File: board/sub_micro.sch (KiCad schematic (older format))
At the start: 0 parts

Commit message: More progress on the schematic. 6502 Done.
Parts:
- added J401: USB_B, symbol Connector_Specialized:USB_B
- added U401: STM32F072CBTx, Package_QFP:LQFP-48_7x7mm_P0.5mm, symbol MCU_ST_STM32:STM32F072CBTx
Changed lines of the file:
@@
 $Descr A4 11693 8268
 encoding utf-8
-Sheet 1 8
+Sheet 3 10
 Title ""
 Date ""
@@
 Comment4 ""
 $EndDescr
+$Comp
+L MCU_ST_STM32:STM32F072CBTx U401
+U 1 1 5AA35B88
+P 5400 3150
+F 0 "U401" H 5400 5228 50  0000 C CNN
+F 1 "STM32F072CBTx" H 5400 5137 50  0000 C CNN
+F 2 "Package_QFP:LQFP-48_7x7mm_P0.5mm" H 9100 4925 50  0001 R TNN
+F 3 "http://www.st.com/st-web-ui/static/active/en/resource/technical/document/datasheet/DM00090510.pdf" H 5400 3150 50  0001 C CNN
+	1    5400 3150
+	1    0    0    -1
+$EndComp
+$Comp
+L Connector_Specialized:USB_B J401
+U 1 1 5AA35CDE
+P 10500 4100
+F 0 "J401" H 10271 4091 50  0000 R CNN
+F 1 "USB_B" H 10271 4000 50  0000 R CNN
+F 2 "" H 10650 4050 50  0001 C CNN
+F 3 "" H 10650 4050 50  0001 C CNN
+	1    10500 4100
+	-1   0    0    -1
+$EndComp
 $EndSCHEMATC

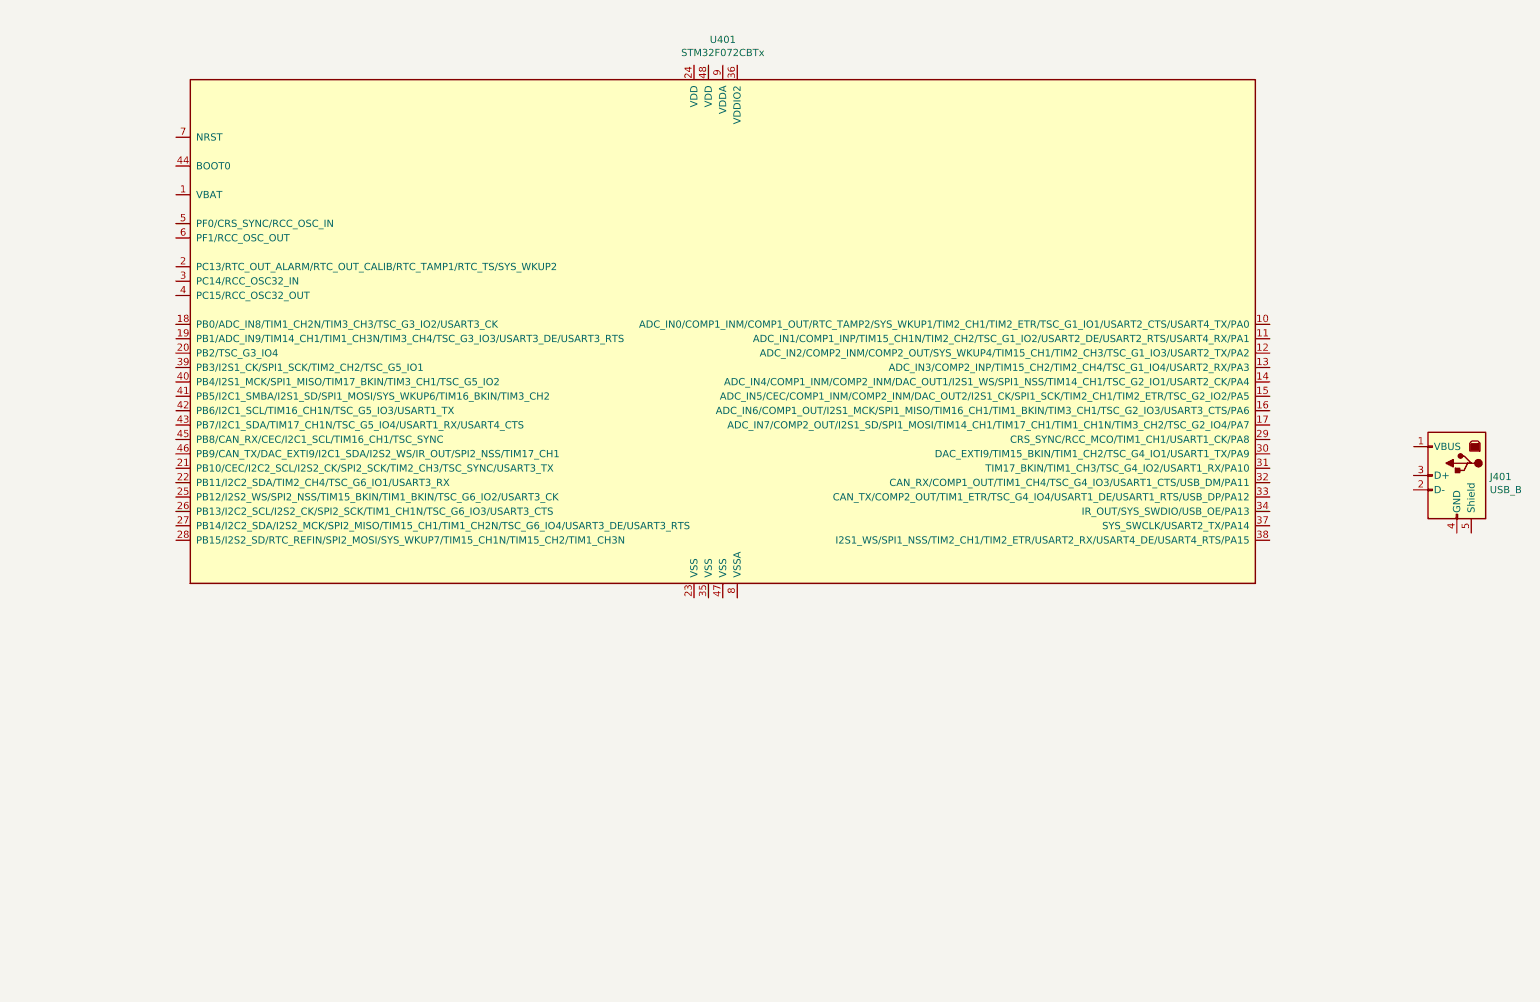
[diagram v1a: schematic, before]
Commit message: Level converters complete, display almost done
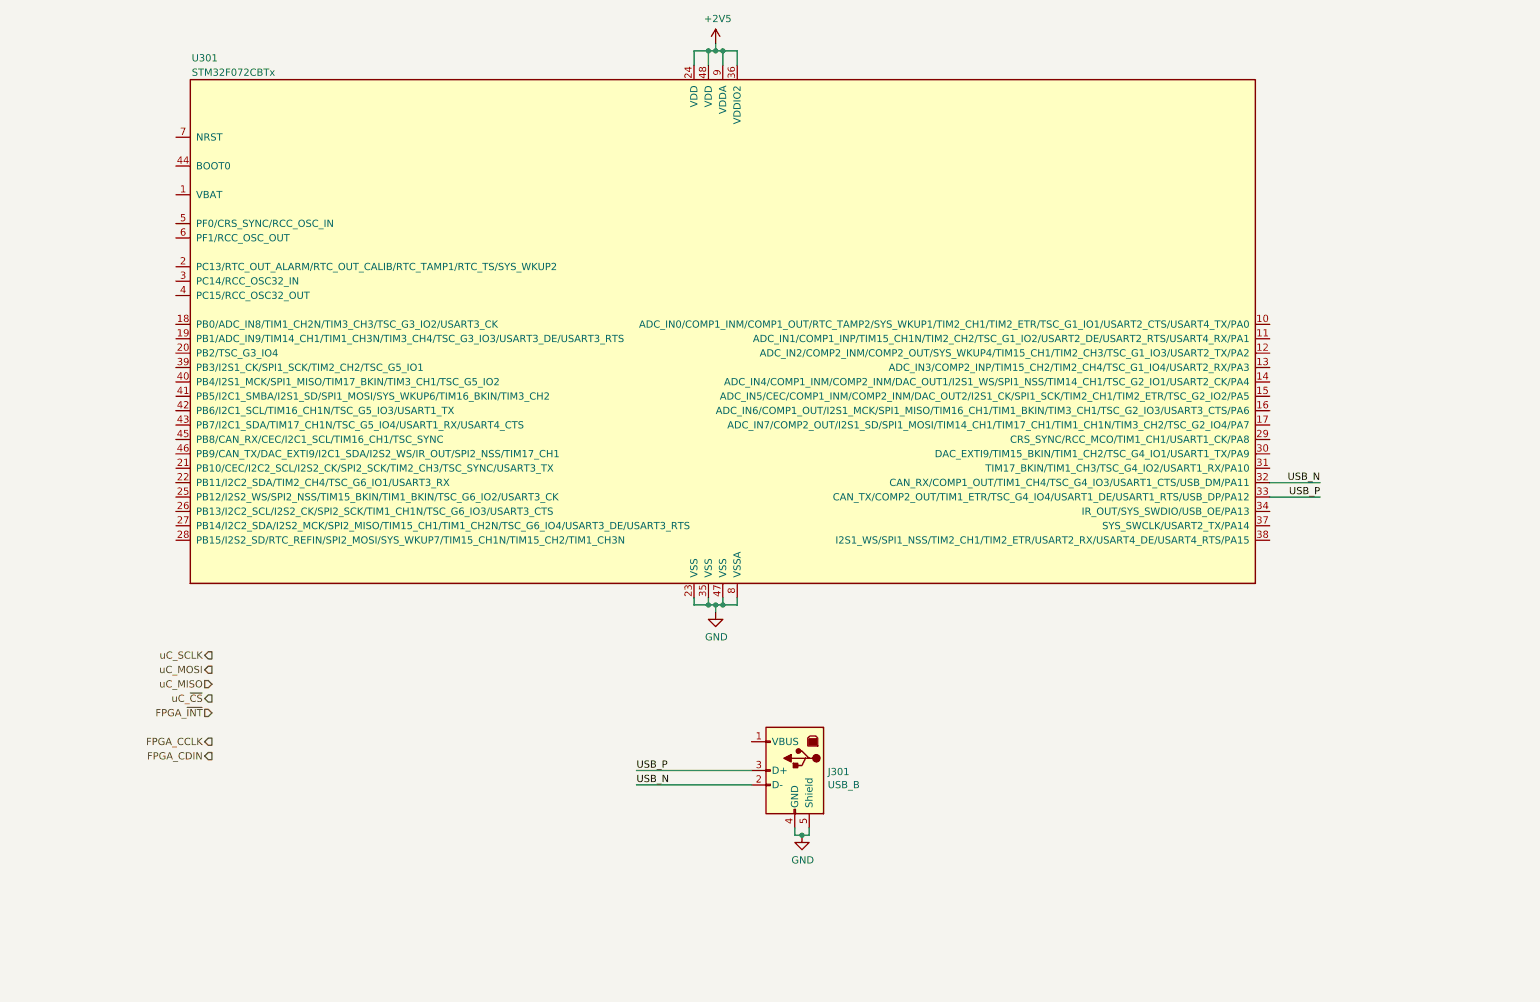
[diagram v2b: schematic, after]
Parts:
- renumbered J401 to J301, U401 to U301
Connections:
- net GND: now reaches U301.23 (VSS)
- net GND: now also J301.4 (GND), J301.5 (Shield), U301.35 (VSS), U301.47 (VSS), U301.8 (VSSA)
- net +2V5: now reaches U301.24 (VDD)
- net +2V5: now also U301.36 (VDDIO2), U301.48 (VDD), U301.9 (VDDA)
- net USB_N: now reaches U301.32 (CAN_RX/COMP1_OUT/TIM1_CH4/TSC_G4_IO3/USART1_CTS/USB_DM/PA11)
- net USB_N: now also J301.2 (D-)
- net USB_P: now reaches U301.33 (CAN_TX/COMP2_OUT/TIM1_ETR/TSC_G4_IO4/USART1_DE/USART1_RTS/USB_DP/PA12)
- net USB_P: now also J301.3 (D+)
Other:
- moved on the sheet: J301
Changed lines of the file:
@@
 $Descr A4 11693 8268
 encoding utf-8
-Sheet 3 10
+Sheet 3 15
 Title ""
 Date ""
@@
 Comment2 ""
 Comment3 ""
-Comment4 ""
+Comment4 "Quokka 6502 Microprocessor Trainer"
 $EndDescr
 $Comp
-L MCU_ST_STM32:STM32F072CBTx U401
+L MCU_ST_STM32:STM32F072CBTx U301
 U 1 1 5AA35B88
 P 5400 3150
-F 0 "U401" H 5400 5228 50  0000 C CNN
-F 1 "STM32F072CBTx" H 5400 5137 50  0000 C CNN
+F 0 "U301" H 1800 5100 50  0000 C CNN
+F 1 "STM32F072CBTx" H 2000 5000 50  0000 C CNN
 F 2 "Package_QFP:LQFP-48_7x7mm_P0.5mm" H 9100 4925 50  0001 R TNN
 F 3 "http://www.st.com/st-web-ui/static/active/en/resource/technical/document/datasheet/DM00090510.pdf" H 5400 3150 50  0001 C CNN
@@
 $EndComp
 $Comp
-L Connector_Specialized:USB_B J401
+L Connector_Specialized:USB_B J301
 U 1 1 5AA35CDE
-P 10500 4100
-F 0 "J401" H 10271 4091 50  0000 R CNN
-F 1 "USB_B" H 10271 4000 50  0000 R CNN
-F 2 "" H 10650 4050 50  0001 C CNN
-F 3 "" H 10650 4050 50  0001 C CNN
-	1    10500 4100
+P 5900 6150
+F 0 "J301" H 5671 6141 50  0000 R CNN
+F 1 "USB_B" H 5671 6050 50  0000 R CNN
+F 2 "" H 6050 6100 50  0001 C CNN
+F 3 "" H 6050 6100 50  0001 C CNN
+	1    5900 6150
 	-1   0    0    -1
 $EndComp
+Text HLabel 1850 5350 0    50   Output ~ 0
+uC_SCLK
+Text HLabel 1850 5450 0    50   Output ~ 0
+uC_MOSI
+Text HLabel 1850 5550 0    50   Input ~ 0
+uC_MISO
+Text HLabel 1850 5650 0    50   Output ~ 0
+uC_~CS
+Text HLabel 1850 5750 0    50   Input ~ 0
+FPGA_~INT
+Text Label 9550 4150 2    50   ~ 0
+USB_N
+Wire Wire Line
+	9200 4150 9550 4150
+Wire Wire Line
+	9200 4250 9550 4250
+Text Label 9550 4250 2    50   ~ 0
+USB_P
+Wire Wire Line
+	5600 6150 4800 6150
+Wire Wire Line
+	5600 6250 4800 6250
+Text Label 4800 6250 0    50   ~ 0
+USB_N
+Text Label 4800 6150 0    50   ~ 0
+USB_P
+$Comp
+L power:GND #PWR0303
+U 1 1 5AA58CA8
+P 5950 6600
+F 0 "#PWR0303" H 5950 6350 50  0001 C CNN
+F 1 "GND" H 5955 6427 50  0000 C CNN
+F 2 "" H 5950 6600 50  0001 C CNN
+F 3 "" H 5950 6600 50  0001 C CNN
+	1    5950 6600
+	1    0    0    -1
+$EndComp
+Wire Wire Line
+	5900 6550 5900 6600
+Wire Wire Line
+	5900 6600 5950 6600
+Wire Wire Line
+	5950 6600 6000 6600
+Wire Wire Line
+	6000 6600 6000 6550
+Connection ~ 5950 6600
+$Comp
+L power:+2V5 #PWR0301
+U 1 1 5AA5F4DD
+P 5350 1100
+F 0 "#PWR0301" H 5350 950 50  0001 C CNN
+F 1 "+2V5" H 5365 1273 50  0000 C CNN
+F 2 "" H 5350 1100 50  0001 C CNN
+F 3 "" H 5350 1100 50  0001 C CNN
+	1    5350 1100
+	1    0    0    -1
+$EndComp
+Wire Wire Line
+	5350 1100 5350 1150
+Wire Wire Line
+	5200 1150 5200 1250
+Wire Wire Line
+	5300 1250 5300 1150
+Wire Wire Line
+	5200 1150 5300 1150
+Connection ~ 5300 1150
+Wire Wire Line
+	5300 1150 5350 1150
+Wire Wire Line
+	5350 1150 5400 1150
+Wire Wire Line
+	5400 1150 5400 1250
+Connection ~ 5350 1150
+Wire Wire Line
+	5400 1150 5500 1150
+Wire Wire Line
+	5500 1150 5500 1250
+Connection ~ 5400 1150
+$Comp
+L power:GND #PWR0302
+U 1 1 5AA5F8A6
+P 5350 5050
+F 0 "#PWR0302" H 5350 4800 50  0001 C CNN
+F 1 "GND" H 5355 4877 50  0000 C CNN
+F 2 "" H 5350 5050 50  0001 C CNN
+F 3 "" H 5350 5050 50  0001 C CNN
+	1    5350 5050
+	1    0    0    -1
+$EndComp
+Wire Wire Line
+	5350 5050 5350 5000
+Wire Wire Line
+	5350 5000 5300 5000
+Wire Wire Line
+	5200 5000 5200 4950
+Wire Wire Line
+	5300 4950 5300 5000
+Connection ~ 5300 5000
+Wire Wire Line
+	5300 5000 5200 5000
+Wire Wire Line
+	5400 4950 5400 5000
+Wire Wire Line
+	5400 5000 5350 5000
+Connection ~ 5350 5000
+Wire Wire Line
+	5500 4950 5500 5000
+Wire Wire Line
+	5500 5000 5400 5000
+Connection ~ 5400 5000
+Text HLabel 1850 5950 0    50   Output ~ 0
+FPGA_CCLK
+Text HLabel 1850 6050 0    50   Output ~ 0
+FPGA_CDIN
 $EndSCHEMATC

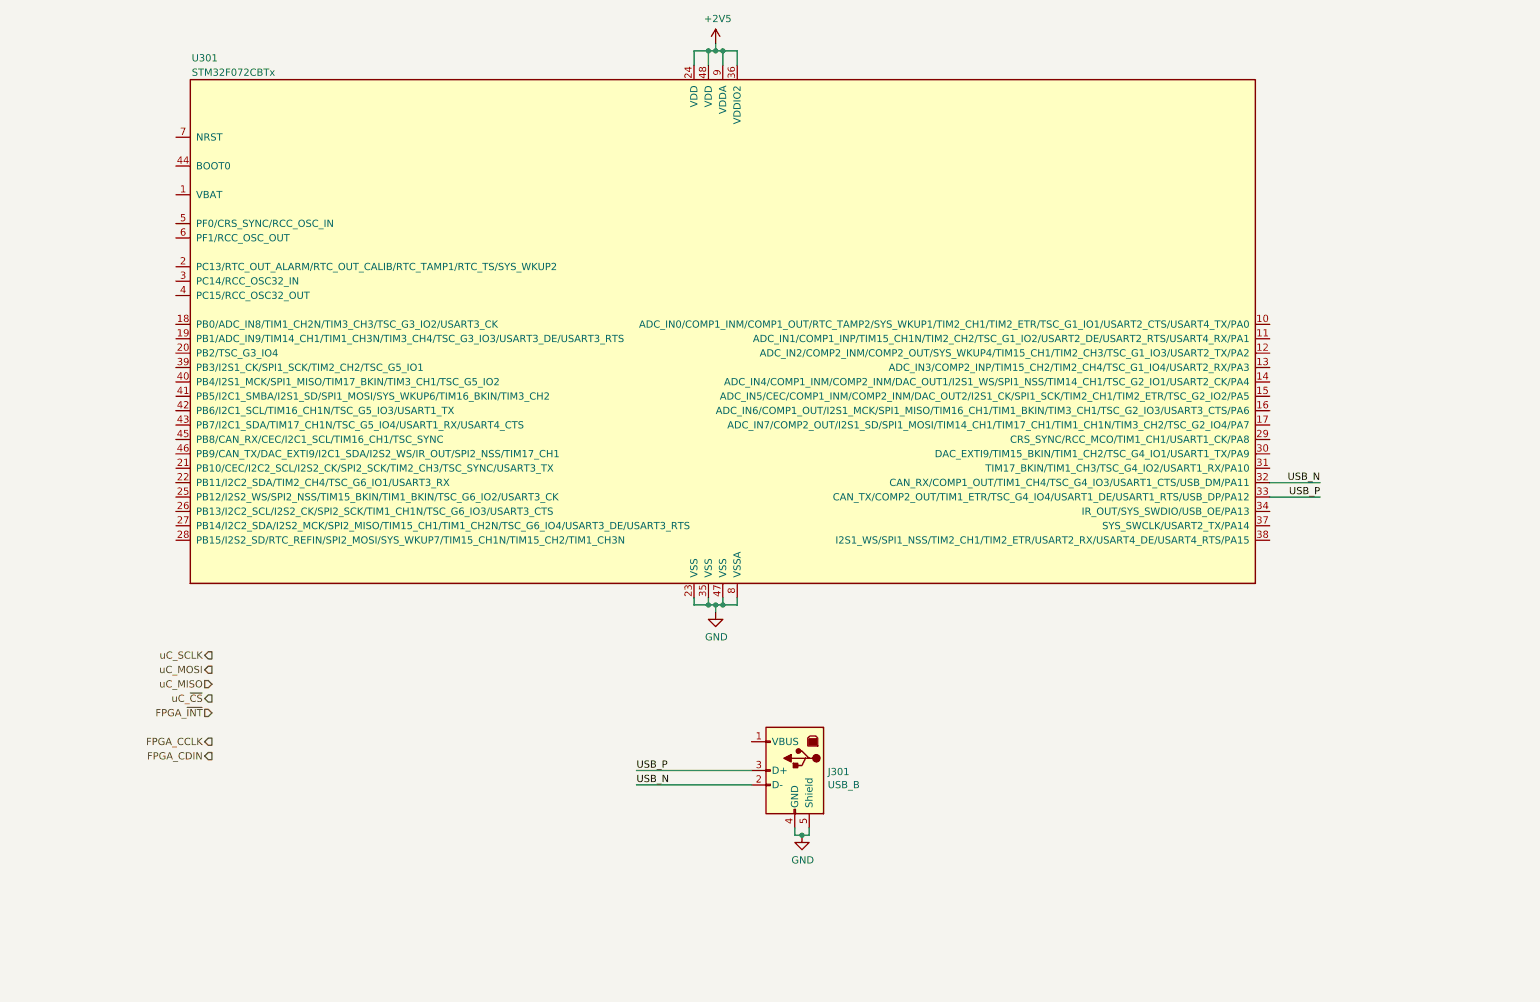
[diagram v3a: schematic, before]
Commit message: Bus signal connectivity rebuilt
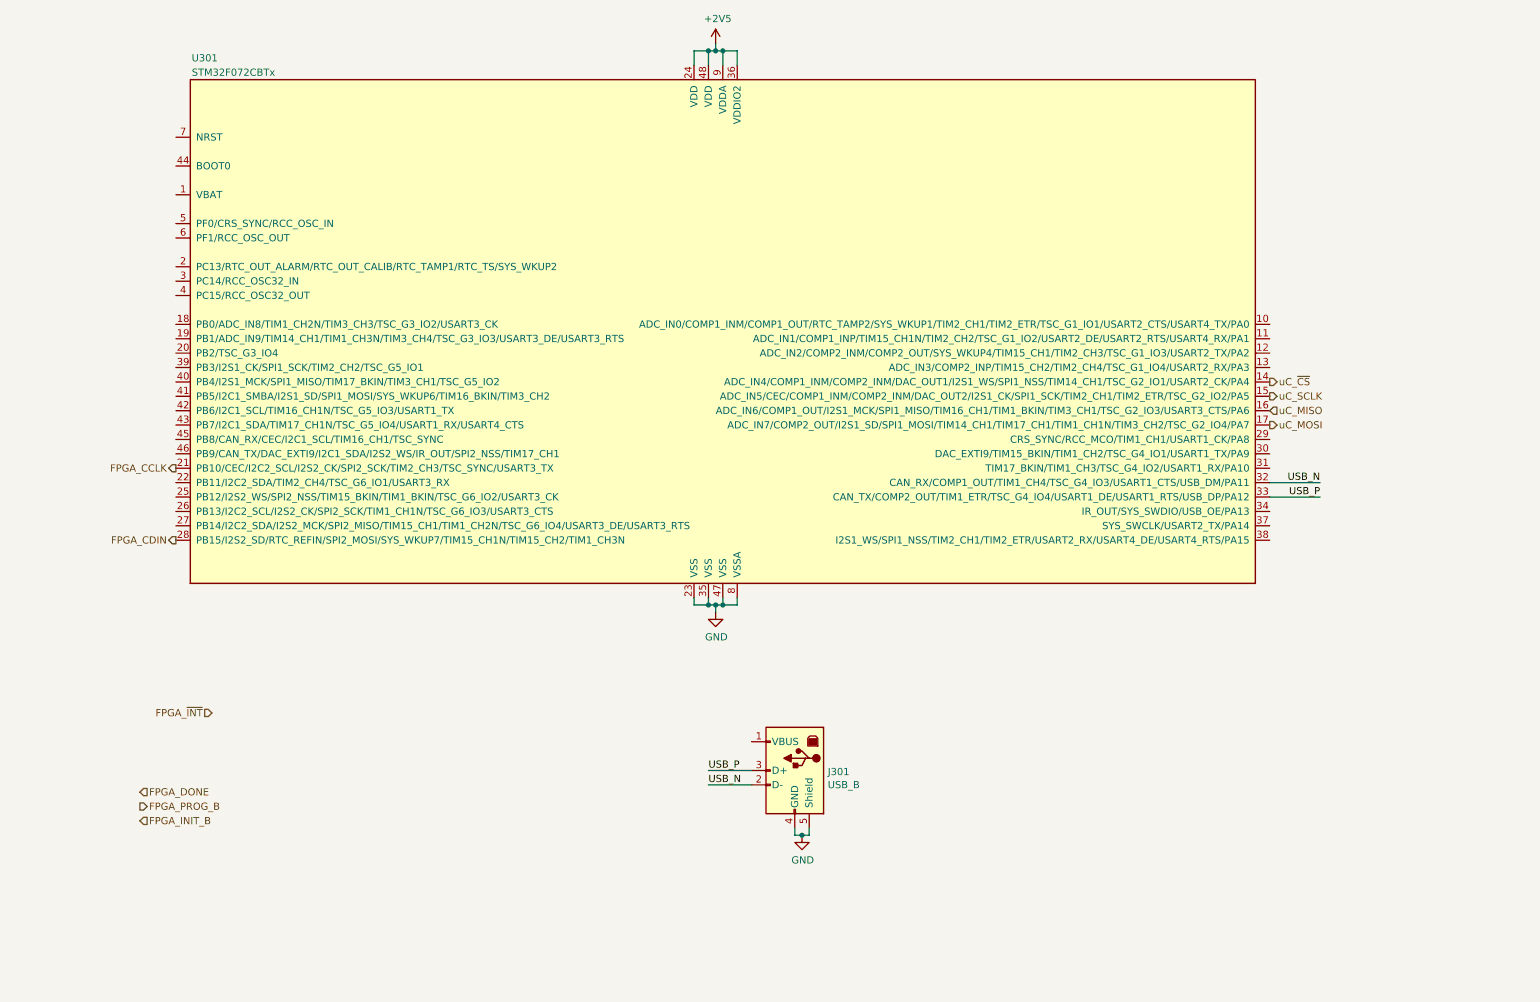
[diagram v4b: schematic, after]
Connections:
- net FPGA_CCLK: now also U301.21 (PB10/CEC/I2C2_SCL/I2S2_CK/SPI2_SCK/TIM2_CH3/TSC_SYNC/USART3_TX)
- net FPGA_CDIN: now also U301.28 (PB15/I2S2_SD/RTC_REFIN/SPI2_MOSI/SYS_WKUP7/TIM15_CH1N/TIM15_CH2/TIM1_CH3N)
- net uC_MISO: now also U301.16 (ADC_IN6/COMP1_OUT/I2S1_MCK/SPI1_MISO/TIM16_CH1/TIM1_BKIN/TIM3_CH1/TSC_G2_IO3/USART3_CTS/PA6)
- net uC_MOSI: now also U301.17 (ADC_IN7/COMP2_OUT/I2S1_SD/SPI1_MOSI/TIM14_CH1/TIM17_CH1/TIM1_CH1N/TIM3_CH2/TSC_G2_IO4/PA7)
- net uC_SCLK: now also U301.15 (ADC_IN5/CEC/COMP1_INM/COMP2_INM/DAC_OUT2/I2S1_CK/SPI1_SCK/TIM2_CH1/TIM2_ETR/TSC_G2_IO2/PA5)
- net uC_~CS: now also U301.14 (ADC_IN4/COMP1_INM/COMP2_INM/DAC_OUT1/I2S1_WS/SPI1_NSS/TIM14_CH1/TSC_G2_IO1/USART2_CK/PA4)
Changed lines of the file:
@@
 	-1   0    0    -1
 $EndComp
-Text HLabel 1850 5350 0    50   Output ~ 0
+Text HLabel 9200 3550 2    50   Output ~ 0
 uC_SCLK
-Text HLabel 1850 5450 0    50   Output ~ 0
+Text HLabel 9200 3750 2    50   Output ~ 0
 uC_MOSI
-Text HLabel 1850 5550 0    50   Input ~ 0
+Text HLabel 9200 3650 2    50   Input ~ 0
 uC_MISO
-Text HLabel 1850 5650 0    50   Output ~ 0
+Text HLabel 9200 3450 2    50   Output ~ 0
 uC_~CS
 Text HLabel 1850 5750 0    50   Input ~ 0
@@
 USB_P
 Wire Wire Line
-	5600 6150 4800 6150
+	5600 6150 5300 6150
 Wire Wire Line
-	5600 6250 4800 6250
-Text Label 4800 6250 0    50   ~ 0
+	5600 6250 5300 6250
+Text Label 5300 6250 0    50   ~ 0
 USB_N
-Text Label 4800 6150 0    50   ~ 0
+Text Label 5300 6150 0    50   ~ 0
 USB_P
 $Comp
@@
 	5500 5000 5400 5000
 Connection ~ 5400 5000
-Text HLabel 1850 5950 0    50   Output ~ 0
+Text HLabel 1600 4050 0    50   Output ~ 0
 FPGA_CCLK
-Text HLabel 1850 6050 0    50   Output ~ 0
+Text HLabel 1600 4550 0    50   Output ~ 0
 FPGA_CDIN
+Text HLabel 1350 6300 2    50   Input ~ 0
+FPGA_DONE
+Text HLabel 1350 6400 2    50   Output ~ 0
+FPGA_PROG_B
+Text HLabel 1350 6500 2    50   Input ~ 0
+FPGA_INIT_B
 $EndSCHEMATC
